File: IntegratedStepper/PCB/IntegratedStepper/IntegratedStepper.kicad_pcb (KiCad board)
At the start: 4 copper layers, 57 x 42.5 mm, 76 parts, among them IC1 DRV8844PWPR, IC2 SN65HVD230DR, IC3 LMR38020FSQDDARQ1, J1 8P8C, J2 8P8C, J3 Screw_Terminal_01x02, J4 Screw_Terminal_01x02, J5 Conn_01x05_Socket, Q1 SS8050-G, Q2 SS8050-G, U1 ESP32-WROOM-32E, U2 AS5048A, U3 CP2102N-Axx-xQFN28

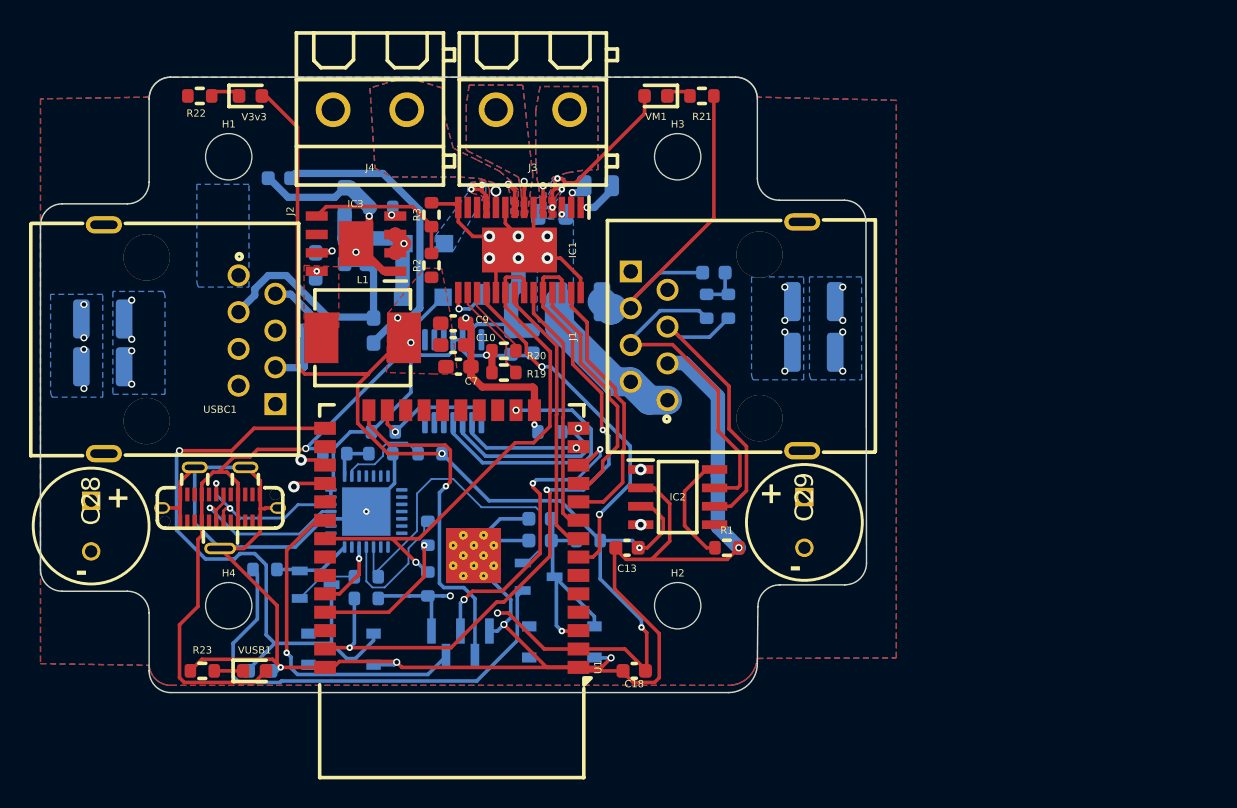
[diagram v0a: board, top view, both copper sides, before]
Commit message: add new libraries
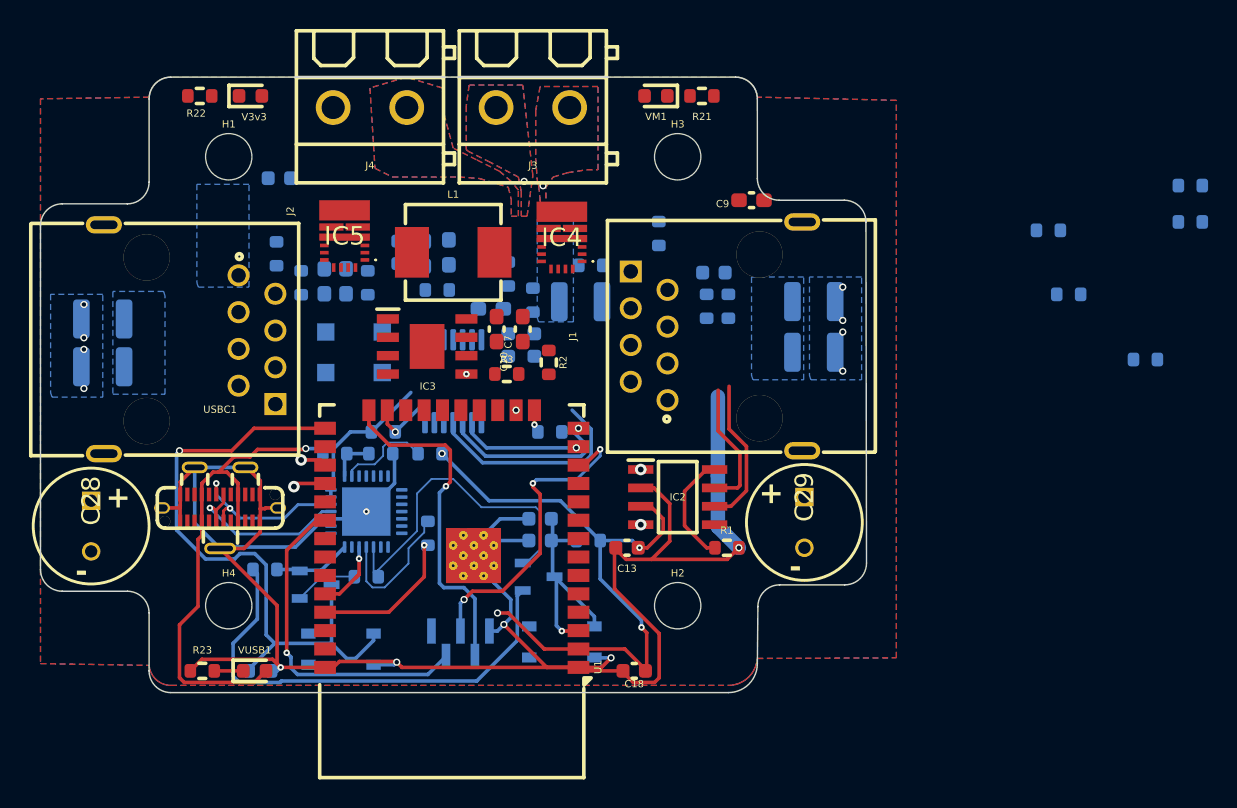
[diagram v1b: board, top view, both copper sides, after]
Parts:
- removed C1, C3: 0.01uF, Capacitor_SMD:C_0805_2012Metric
- removed C2: 0.1uF, Capacitor_SMD:C_0805_2012Metric
- removed IC1: DRV8844PWPR, SamacSys_Parts:SOP65P640X120-29N
- removed R17, R18, R19, R20: 2k, Resistor_SMD:R_0603_1608Metric
- added IC4: DRV8243HQRXYRQ1, SamacSys_Parts:DRV8243HQRXYRQ1, F.Cu at (128.5, 111.1)
- added IC5: DRV8243HQRXYRQ1, SamacSys_Parts:DRV8243HQRXYRQ1, F.Cu at (113.5, 111.0)
- added R_DIAG1: 8.2k, Resistor_SMD:R_0603_1608Metric, B.Cu at (124.8, 113.6)
- added R_DIAG2: 8.2k, Resistor_SMD:R_0603_1608Metric, B.Cu at (110.5, 114.2)
- added R_DRV1: 2k, Resistor_SMD:R_0603_1608Metric, B.Cu at (168.8, 119.5)
- added R_IPROP1: 820, Resistor_SMD:R_0603_1608Metric, B.Cu at (135.2, 110.8)
- added R_IPROP2: 820, Resistor_SMD:R_0603_1608Metric, B.Cu at (108.8, 112.2)
- added R_MODE1: 8.2k, Resistor_SMD:R_0603_1608Metric, B.Cu at (130.5, 113.0)
- added R_MODE2: 8.2k, Resistor_SMD:R_0603_1608Metric, B.Cu at (115.1, 114.2)
- added R_SLEEP1: 2k, Resistor_SMD:R_0603_1608Metric, B.Cu at (126.5, 115.4)
- added R_SR1: 8.2k, Resistor_SMD:R_0603_1608Metric, B.Cu at (163.5, 115.0)
- added R_SR2: 8.2k, Resistor_SMD:R_0603_1608Metric, B.Cu at (162.1, 110.6)
- added R_nFAULT_1: 2k, Resistor_SMD:R_0603_1608Metric, B.Cu at (171.9, 107.5)
- added R_nFAULT_2: 2k, Resistor_SMD:R_0603_1608Metric, B.Cu at (171.9, 110.0)
- moved C9 22.3 mm to (141.6, 108.5), turned to 180 degrees
- moved C11 12.5 mm to (123.6, 116.0), turned to 180 degrees
- moved R3 12.2 mm to (124.7, 120.5), turned to 0 degrees
- moved R2 10.5 mm to (127.6, 119.7), turned to -90 degrees
- moved IC3 8.63 mm to (119.2, 118.6), turned to 0 degrees
- moved L1 8.59 mm to (121.0, 112.1)
- moved D1 8.04 mm to (116.1, 119.0), turned to -90 degrees
- moved C25 7.84 mm to (117.2, 112.1), turned to 90 degrees
- moved D2 7.70 mm to (112.2, 119.0), turned to -90 degrees
- moved C8 7.50 mm to (120.7, 112.1), turned to -90 degrees
- moved R4 6.91 mm to (119.9, 114.7), turned to 0 degrees
- moved C6 6.63 mm to (119.0, 112.2)
- moved C7 5.14 mm to (125.8, 117.4), turned to -90 degrees
- moved C4 3.58 mm to (112.1, 114.1), turned to -90 degrees
- moved C10 3.20 mm to (124.0, 117.4), turned to -90 degrees
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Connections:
- net VCC renamed /3V3_VReg/VM
- U1 pad 26: unconnected-(U1-IO4-Pad26) -> /DRV8844/DRVOFF
- U1 pad 29: unconnected-(U1-IO5-Pad29) -> /DRV8844/NSLEEP
- U1 pad 31: /DRV8844/EN3 -> /DRV8844/NFAULT_1
- U1 pad 37: /DRV8844/EN1 -> /DRV8844/NFAULT_2
- U1 pad 6: unconnected-(U1-IO34-Pad6) -> IPROPI_1
- U1 pad 7: /DRV8844/NFAULT -> IPROPI_2
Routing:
- net GND: track 269.4 -> 162.7 mm, vias 24 -> 15
- net 3V3_VCC: track 141.2 -> 57.7 mm, vias 8 -> 4
- net /DRV8844/EN1: track 48.4 -> 0.00 mm, vias 3 -> 0
- net /DRV8844/EN3: track 35.9 -> 0.00 mm, vias 1 -> 0
- net /3V3_VReg/VM: track 40.0 -> 6.13 mm, vias 13 -> 0
- net /DRV8844/NFAULT: track 24.9 -> 0.00 mm, vias 2 -> 0
- net /DRV8844/IN4: track 19.2 -> 0.00 mm
- net /DRV8844/IN1: track 18.3 -> 0.00 mm
- net /DRV8844/IN3: track 17.4 -> 0.00 mm
- net /DRV8844/IN2: track 16.6 -> 0.00 mm
- net V_USB: track 48.7 -> 34.3 mm
- net CANL: track 48.4 -> 34.6 mm
- net VIN: track 11.5 -> 0.00 mm, vias 1 -> 0
- net CANH: track 52.8 -> 41.8 mm
- net Net-(IC3-FB): track 10.7 -> 0.00 mm, vias 0 -> 1
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- removed copper zone on F.Cu, net /3V3_VReg/VM
- removed copper zone on F.Cu, net 3V3_VCC
- removed copper zone on F.Cu, net Net-(IC3-SW)
